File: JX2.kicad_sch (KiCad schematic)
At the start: 1 part

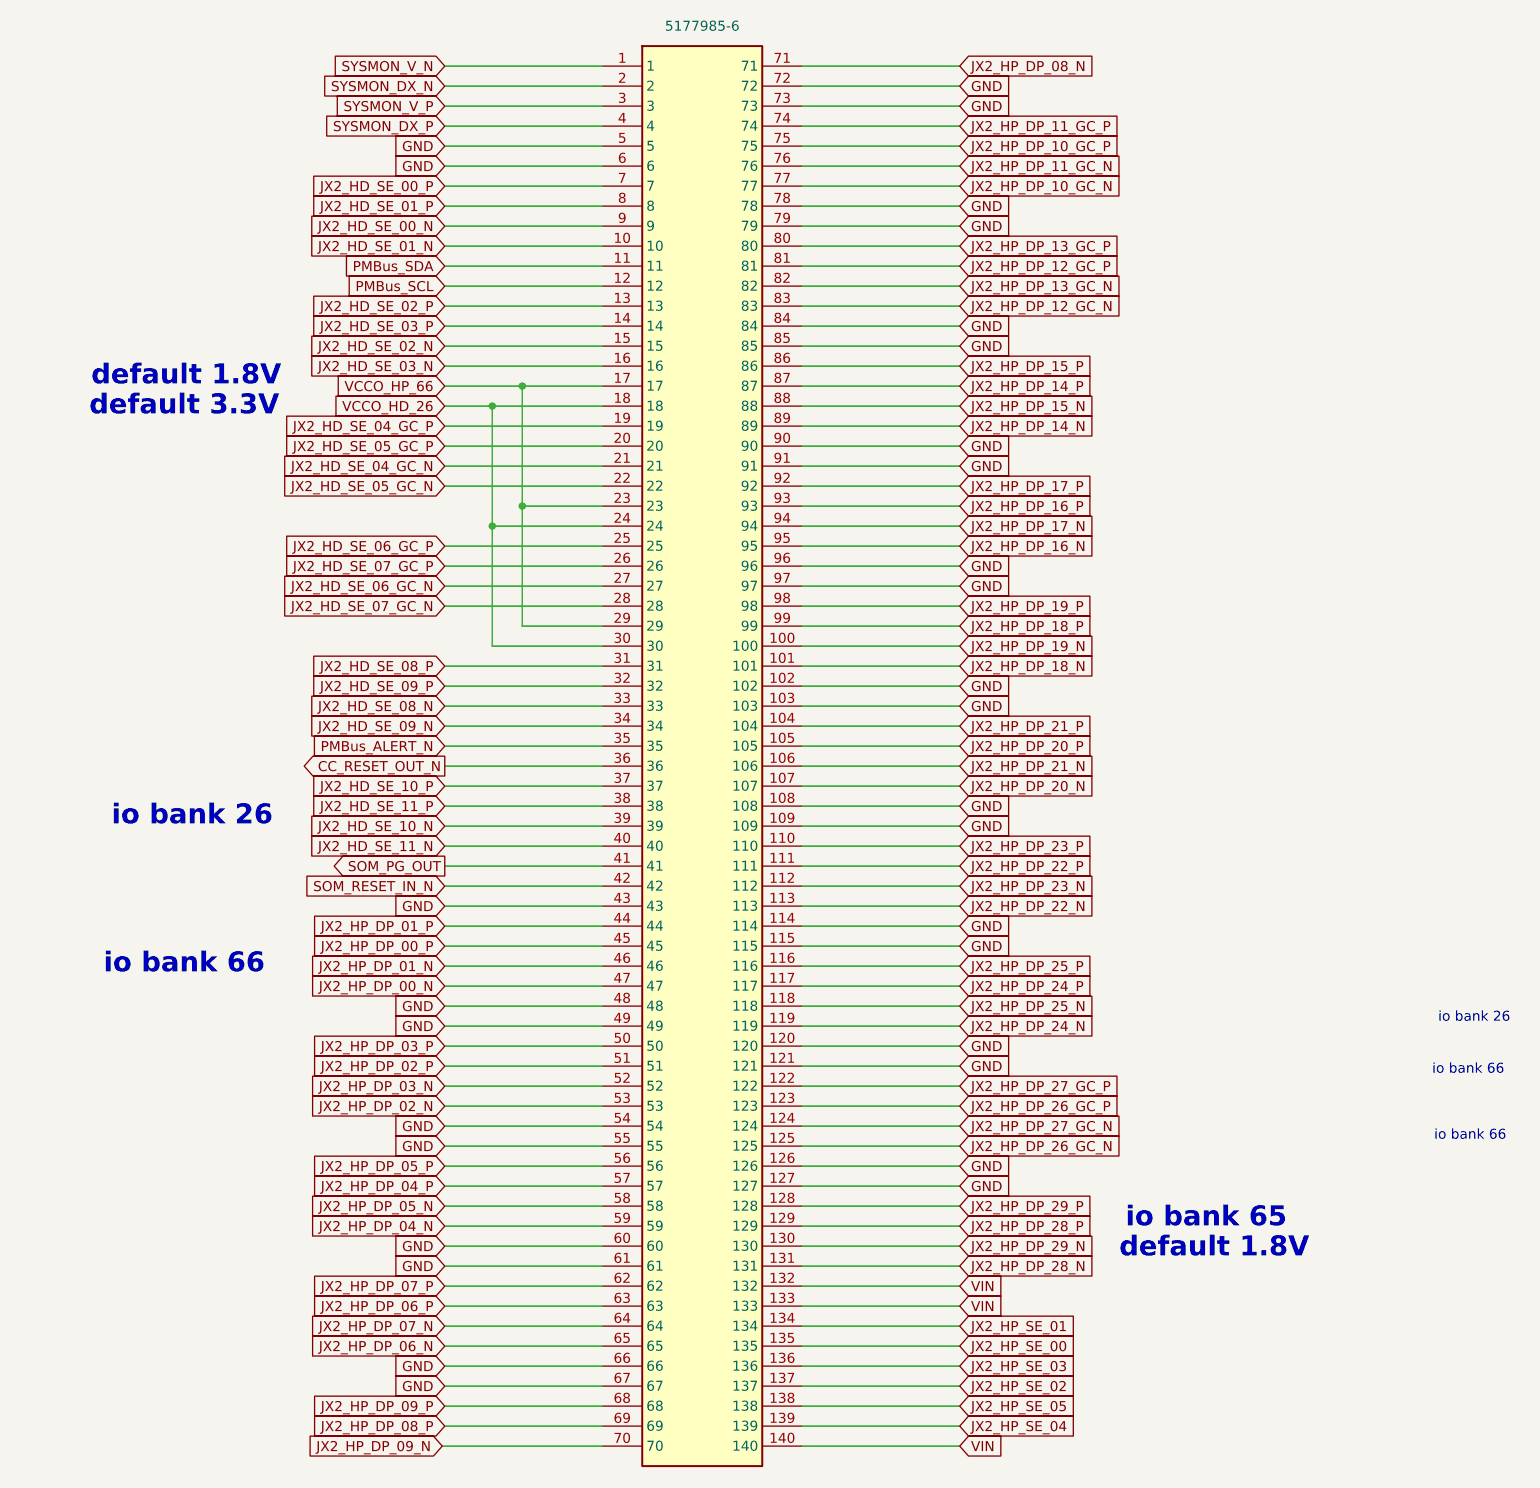
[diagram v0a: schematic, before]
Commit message: moved jtag connector, added holes for all power supplies, fixed most of DRC
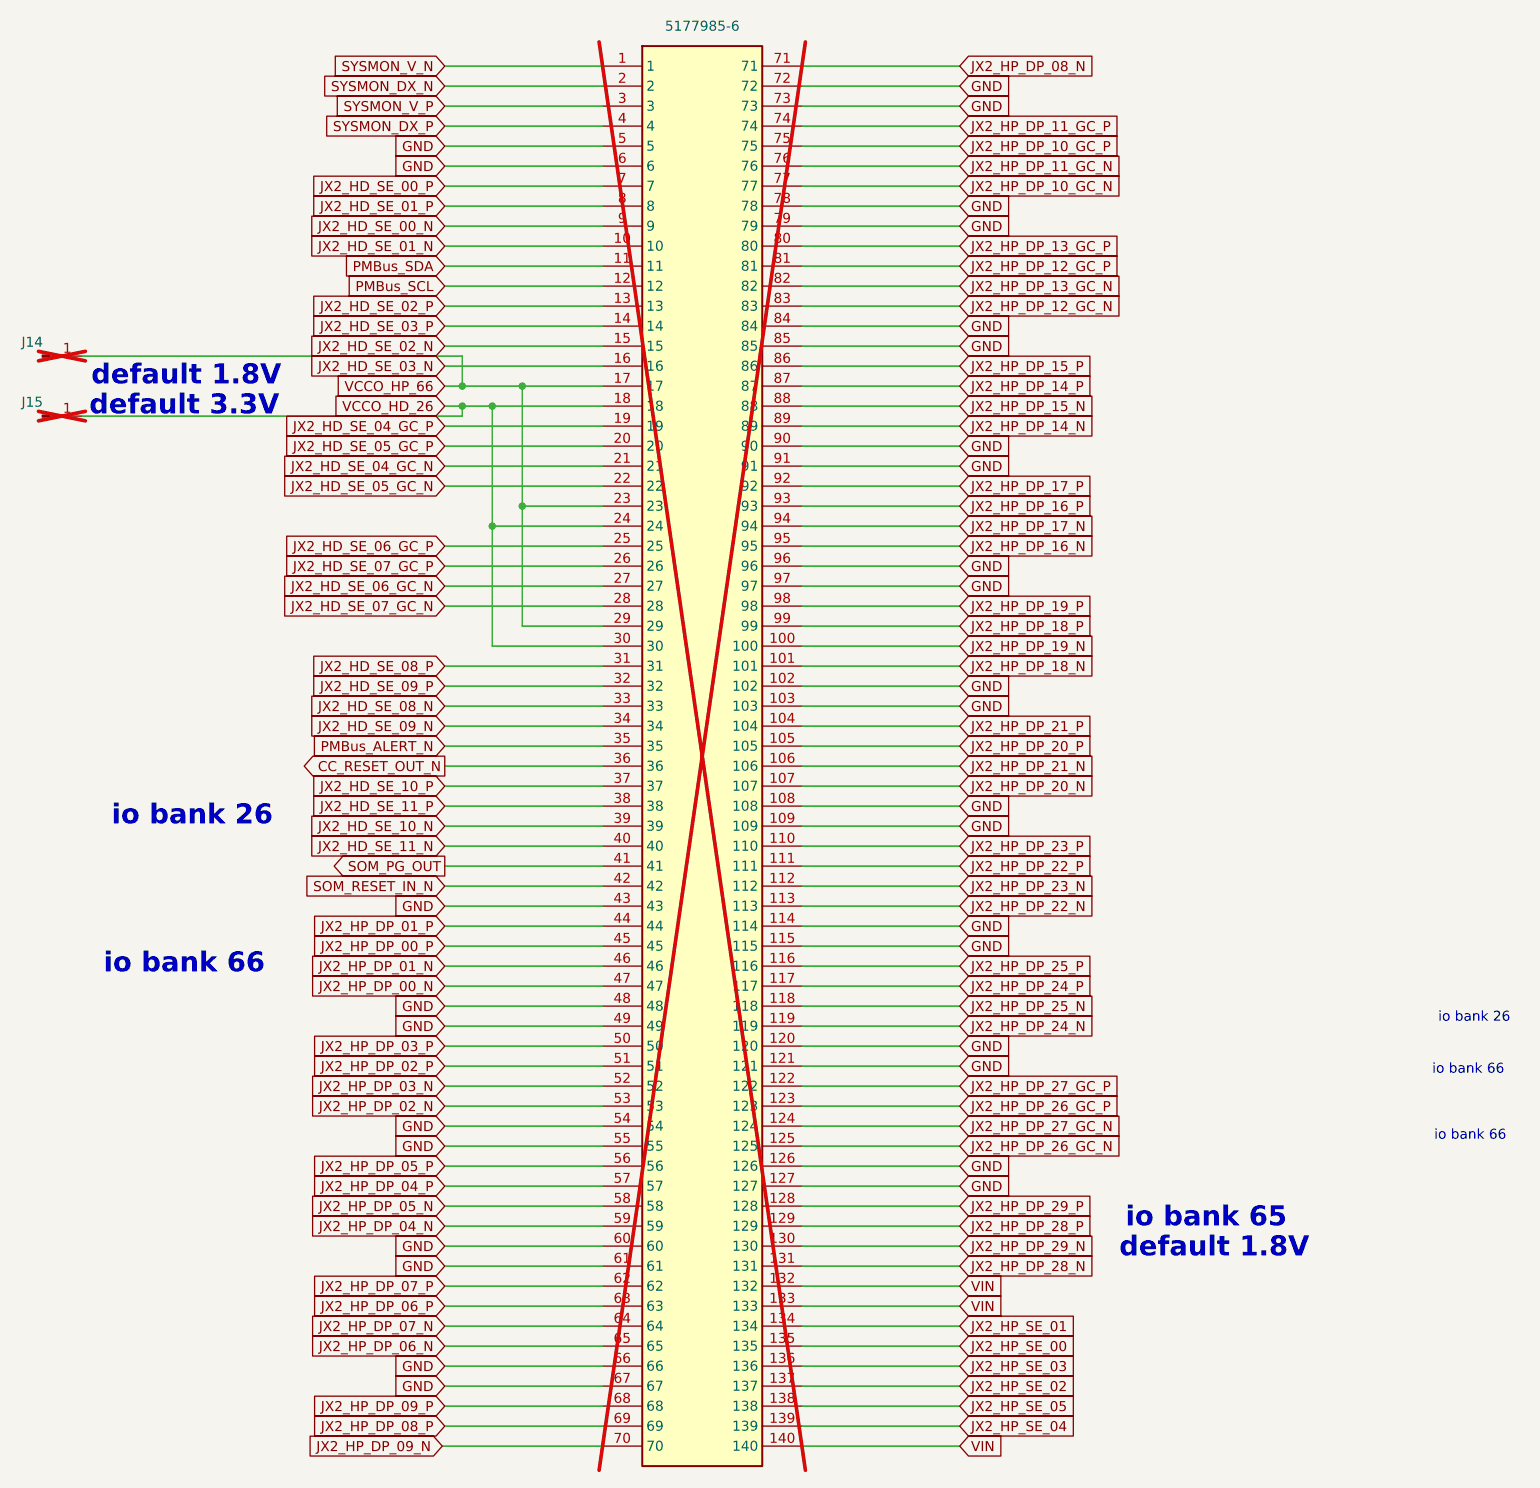
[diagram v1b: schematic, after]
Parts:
- added J14, J15: Conn_01x01_Pin, Connector_PinHeader_2.00mm:PinHeader_1x01_P2.00mm_Horizontal, symbol Connector:Conn_01x01_Pin
- JX2: now not fitted
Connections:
- net VCCO_HD_26: now also J15.1 (Pin_1)
- net VCCO_HP_66: now also J14.1 (Pin_1)
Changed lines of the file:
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@@
 	(paper "A4")
 	(junction
+		(at 78.74 59.69)
+		(diameter 0)
+		(color 0 0 0 0)
+	)
+	(junction
 		(at 86.36 57.15)
 		(diameter 0)
@@
 	)
 	(junction
+		(at 78.74 57.15)
+		(diameter 0)
+		(color 0 0 0 0)
+	)
+	(junction
 		(at 86.36 72.39)
 		(diameter 0)
@@
 	(wire
 		(pts
-			(xy 82.55 59.69) (xy 76.52 59.69)
+			(xy 82.55 59.69) (xy 78.74 59.69)
 		)
 		(stroke
@@
 	(wire
 		(pts
+			(xy 30.48 60.96) (xy 78.74 60.96)
+		)
+		(stroke
+			(width 0)
+			(type default)
+		)
+	)
+	(wire
+		(pts
 			(xy 121.92 179.07) (xy 141.92 179.07)
 		)
@@
 	(wire
 		(pts
+			(xy 78.74 60.96) (xy 78.74 59.69)
+		)
+		(stroke
+			(width 0)
+			(type default)
+		)
+	)
+	(wire
+		(pts
 			(xy 96.52 90.17) (xy 82.55 90.17)
 		)
@@
 	(wire
 		(pts
-			(xy 86.36 57.15) (xy 76.52 57.15)
+			(xy 86.36 57.15) (xy 78.74 57.15)
+		)
+		(stroke
+			(width 0)
+			(type default)
+		)
+	)
+	(wire
+		(pts
+			(xy 78.74 59.69) (xy 76.52 59.69)
 		)
 		(stroke
@@
 	(wire
 		(pts
+			(xy 30.48 53.34) (xy 78.74 53.34)
+		)
+		(stroke
+			(width 0)
+			(type default)
+		)
+	)
+	(wire
+		(pts
 			(xy 121.92 46.99) (xy 141.92 46.99)
 		)
@@
 	(wire
 		(pts
+			(xy 78.74 53.34) (xy 78.74 57.15)
+		)
+		(stroke
+			(width 0)
+			(type default)
+		)
+	)
+	(wire
+		(pts
+			(xy 78.74 57.15) (xy 76.52 57.15)
+		)
+		(stroke
+			(width 0)
+			(type default)
+		)
+	)
+	(wire
+		(pts
 			(xy 96.52 34.29) (xy 76.52 34.29)
 		)
@@
 	)
 	(symbol
+		(lib_id "Connector:Conn_01x01_Pin")
+		(at 25.4 60.96 0)
+		(unit 1)
+		(exclude_from_sim no)
+		(in_bom yes)
+		(on_board yes)
+		(dnp yes)
+		(property "Reference" "J15"
+			(at 24.13 59.182 0)
+			(effects
+				(font
+					(size 1.27 1.27)
+				)
+			)
+		)
+		(property "Value" "Conn_01x01_Pin"
+			(at 12.446 62.484 0)
+			(effects
+				(font
+					(size 1.27 1.27)
+				)
+				(hide yes)
+			)
+		)
+		(property "Footprint" "Connector_PinHeader_2.00mm:PinHeader_1x01_P2.00mm_Horizontal"
+			(at 25.4 60.96 0)
+			(effects
+				(font
+					(size 1.27 1.27)
+				)
+				(hide yes)
+			)
+		)
+		(property "Datasheet" "~"
+			(at 25.4 60.96 0)
+			(effects
+				(font
+					(size 1.27 1.27)
+				)
+				(hide yes)
+			)
+		)
+		(property "Description" "Generic connector, single row, 01x01, script generated"
+			(at 25.4 60.96 0)
+			(effects
+				(font
+					(size 1.27 1.27)
+				)
+				(hide yes)
+			)
+		)
+		(pin "1"
+		)
+		(instances
+			(project "simpleCarrier"
+				(path "/72db9dae-5f31-4a10-9047-fdf9bc345a06/c93acd63-62f0-4482-8389-61a1d7f7d90f"
+					(reference "J15")
+					(unit 1)
+				)
+			)
+		)
+	)
+	(symbol
+		(lib_id "Connector:Conn_01x01_Pin")
+		(at 25.4 53.34 0)
+		(unit 1)
+		(exclude_from_sim no)
+		(in_bom yes)
+		(on_board yes)
+		(dnp yes)
+		(property "Reference" "J14"
+			(at 24.13 51.562 0)
+			(effects
+				(font
+					(size 1.27 1.27)
+				)
+			)
+		)
+		(property "Value" "Conn_01x01_Pin"
+			(at 12.446 54.864 0)
+			(effects
+				(font
+					(size 1.27 1.27)
+				)
+				(hide yes)
+			)
+		)
+		(property "Footprint" "Connector_PinHeader_2.00mm:PinHeader_1x01_P2.00mm_Horizontal"
+			(at 25.4 53.34 0)
+			(effects
+				(font
+					(size 1.27 1.27)
+				)
+				(hide yes)
+			)
+		)
+		(property "Datasheet" "~"
+			(at 25.4 53.34 0)
+			(effects
+				(font
+					(size 1.27 1.27)
+				)
+				(hide yes)
+			)
+		)
+		(property "Description" "Generic connector, single row, 01x01, script generated"
+			(at 25.4 53.34 0)
+			(effects
+				(font
+					(size 1.27 1.27)
+				)
+				(hide yes)
+			)
+		)
+		(pin "1"
+		)
+		(instances
+			(project "simpleCarrier"
+				(path "/72db9dae-5f31-4a10-9047-fdf9bc345a06/c93acd63-62f0-4482-8389-61a1d7f7d90f"
+					(reference "J14")
+					(unit 1)
+				)
+			)
+		)
+	)
+	(symbol
 		(lib_id "SamacSys_Parts:5177985-6")
 		(at 96.52 16.51 0)
@@
 		(in_bom yes)
 		(on_board yes)
-		(dnp no)
+		(dnp yes)
 		(fields_autoplaced yes)
 		(property "Reference" "JX2"
